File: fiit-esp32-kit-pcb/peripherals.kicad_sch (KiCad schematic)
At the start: 21 parts, among them Q2 SFH320, SW1 SPST NO, SW2 SPST NO, SW3 SPST NO, SW4 SPST NO, U4 AHT20

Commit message: footprints assignment
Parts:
- removed U4: AHT20, Findemm:AHT20, symbol Findemm:AHT20
- added U4: AHT20, FIIT_Kit:AHT20, symbol FIIT_Kit:AHT20
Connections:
- net +3.3V: now also U4.2 (VDD)
- net GND: now also U4.5 (GND)
- net SCL: now also U4.3 (SCL)
- net SDA: now also U4.4 (SDA)
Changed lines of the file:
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@@
+	)
+	(symbol
+		(lib_id "FIIT_Kit:AHT20")
+		(at 101.6 132.08 0)
+		(unit 1)
+		(exclude_from_sim no)
+		(in_bom yes)
+		(on_board yes)
+		(dnp no)
+		(property "Reference" "U4"
+			(at 93.726 121.412 0)
+			(effects
+				(font
+					(size 1.27 1.27)
+				)
+				(justify left)
+			)
+		)
+		(property "Value" "AHT20"
+			(at 93.726 123.444 0)
+			(effects
+				(font
+					(size 1.27 1.27)
+				)
+				(justify left)
+			)
+		)
+		(property "Footprint" "FIIT_Kit:AHT20"
+			(at 101.6 132.08 0)
+			(effects
+				(font
+					(size 1.27 1.27)
+				)
+				(justify bottom)
+				(hide yes)
+			)
+		)
+		(property "Datasheet" "https://files.seeedstudio.com/wiki/Grove-AHT20_I2C_Industrial_Grade_Temperature_and_Humidity_Sensor/AHT20-datasheet-2020-4-16.pdf"
+			(at 101.6 132.08 0)
+			(effects
+				(font
+					(size 1.27 1.27)
+				)
+				(hide yes)
+			)
+		)
+		(property "Description" ""
+			(at 101.6 132.08 0)
+			(effects
+				(font
+					(size 1.27 1.27)
+				)
+				(hide yes)
+			)
+		)
+		(property "LCSC" "C2757850"
+			(at 101.6 132.08 0)
+			(effects
+				(font
+					(size 1.27 1.27)
+				)
+				(hide yes)
+			)
+		)
+		(property "Manufacturer Part Number" "AHT20"
+			(at 101.6 132.08 0)
+			(effects
+				(font
+					(size 1.27 1.27)
+				)
+				(hide yes)
+			)
+		)
+		(pin "4"
+		)
+		(pin "3"
+		)
+		(pin "1"
+		)
+		(pin "2"
+		)
+		(pin "5"
+		)
+		(pin "6"
+		)
+		(instances
+			(project ""
+				(path "/d7013812-ce13-4db9-a6cc-42acdc5acaf9/fe4defb8-cb63-4770-8d91-1c7f8da70e07"
+					(reference "U4")
+					(unit 1)
+				)
+			)
+		)
 	)
 	(symbol
@@
 					(unit 1)
 				)
-			)
-		)
-	)
-	(symbol
-		(lib_id "Findemm:AHT20")
-		(at 101.6 132.08 0)
-		(unit 1)
-		(exclude_from_sim no)
-		(in_bom yes)
-		(on_board yes)
-		(dnp no)
-		(property "Reference" "U4"
-			(at 93.472 121.158 0)
-			(effects
-				(font
-					(size 1.27 1.27)
-				)
-				(justify left)
-			)
-		)
-		(property "Value" "AHT20"
-			(at 93.472 123.19 0)
-			(effects
-				(font
-					(size 1.27 1.27)
-				)
-				(justify left)
-			)
-		)
-		(property "Footprint" "Findemm:AHT20"
-			(at 101.6 132.08 0)
-			(effects
-				(font
-					(size 1.27 1.27)
-				)
-				(justify bottom)
-				(hide yes)
-			)
-		)
-		(property "Datasheet" "https://files.seeedstudio.com/wiki/Grove-AHT20_I2C_Industrial_Grade_Temperature_and_Humidity_Sensor/AHT20-datasheet-2020-4-16.pdf"
-			(at 101.6 132.08 0)
-			(effects
-				(font
-					(size 1.27 1.27)
-				)
-				(hide yes)
-			)
-		)
-		(property "Description" ""
-			(at 101.6 132.08 0)
-			(effects
-				(font
-					(size 1.27 1.27)
-				)
-				(hide yes)
-			)
-		)
-		(property "LCSC" "C2757850"
-			(at 101.6 132.08 0)
-			(effects
-				(font
-					(size 1.27 1.27)
-				)
-				(hide yes)
-			)
-		)
-		(property "Manufacturer Part Number" "AHT20"
-			(at 101.6 132.08 0)
-			(effects
-				(font
-					(size 1.27 1.27)
-				)
-				(hide yes)
-			)
-		)
-		(pin "2"
-		)
-		(pin "3"
-		)
-		(pin "4"
-		)
-		(pin "5"
-		)
-		(pin "1"
-		)
-		(pin "6"
-		)
-		(instances
-			(project "fiit-esp32-kit-pcb"
-				(path "/d7013812-ce13-4db9-a6cc-42acdc5acaf9/fe4defb8-cb63-4770-8d91-1c7f8da70e07"
-					(reference "U4")
-					(unit 1)
-				)

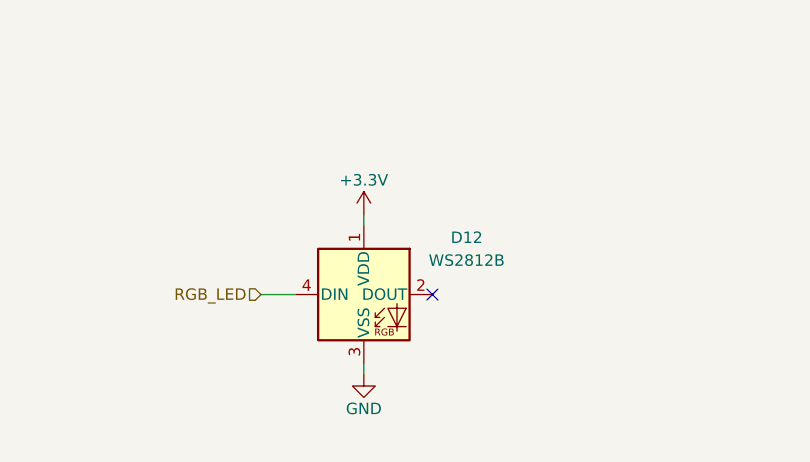
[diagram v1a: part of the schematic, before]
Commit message: updated manufacturer part numbers
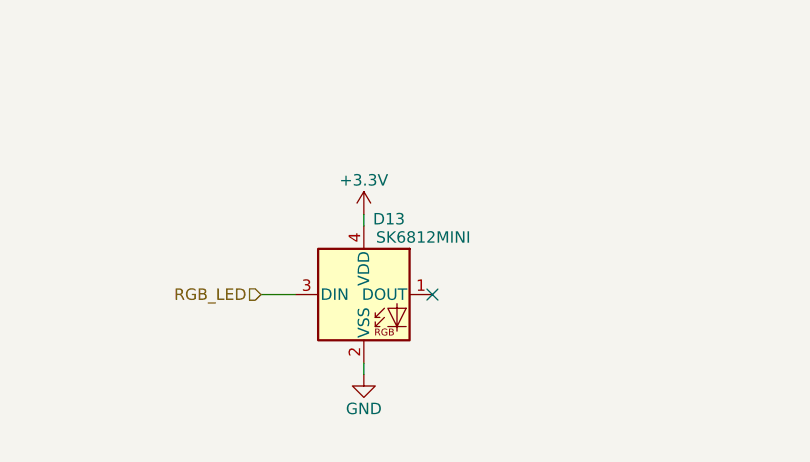
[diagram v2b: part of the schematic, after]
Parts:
- removed D12: WS2812B, LED_SMD:LED_WS2812B_PLCC4_5.0x5.0mm_P3.2mm, symbol LED:WS2812B
- added D13: SK6812MINI, LED_SMD:LED_SK6812MINI_PLCC4_3.5x3.5mm_P1.75mm, symbol LED:SK6812MINI
- Q2: footprint LED_SMD:LED_PLCC-2_3.4x3.0mm_KA -> FIIT_Kit:TEMT6000X01; LCSC (none) -> C94098; Manufacturer Part Number (none) -> TEMT6000X01
- R20, R21, R23, R26: LCSC (none) -> C22775; Manufacturer Part Number (none) -> 0603WAF1000T5E
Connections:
- net +3.3V: now also D13.4 (VDD)
- net GND: now also D13.2 (VSS)
- net RGB_LED: now also D13.3 (DIN)
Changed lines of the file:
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@@
 			)
 		)
-		(property "LCSC" ""
+		(property "LCSC" "C22775"
 			(at 152.4 60.96 0)
 			(effects
@@
 			)
 		)
-		(property "Manufacturer Part Number" ""
+		(property "Manufacturer Part Number" "0603WAF1000T5E"
 			(at 152.4 60.96 0)
 			(effects
@@
 			)
 		)
-		(property "LCSC" ""
+		(property "LCSC" "C22775"
 			(at 152.4 52.07 0)
 			(effects
@@
 			)
 		)
-		(property "Manufacturer Part Number" ""
+		(property "Manufacturer Part Number" "0603WAF1000T5E"
 			(at 152.4 52.07 0)
 			(effects
@@
 				(path "/d7013812-ce13-4db9-a6cc-42acdc5acaf9/fe4defb8-cb63-4770-8d91-1c7f8da70e07"
 					(reference "#PWR058")
-					(unit 1)
-				)
-			)
-		)
-	)
-	(symbol
-		(lib_id "LED:WS2812B")
-		(at 195.58 133.35 0)
-		(unit 1)
-		(exclude_from_sim no)
-		(in_bom yes)
-		(on_board yes)
-		(dnp no)
-		(fields_autoplaced yes)
-		(property "Reference" "D12"
-			(at 207.01 127.0314 0)
-			(effects
-				(font
-					(size 1.27 1.27)
-				)
-			)
-		)
-		(property "Value" "WS2812B"
-			(at 207.01 129.5714 0)
-			(effects
-				(font
-					(size 1.27 1.27)
-				)
-			)
-		)
-		(property "Footprint" "LED_SMD:LED_WS2812B_PLCC4_5.0x5.0mm_P3.2mm"
-			(at 196.85 140.97 0)
-			(effects
-				(font
-					(size 1.27 1.27)
-				)
-				(justify left top)
-				(hide yes)
-			)
-		)
-		(property "Datasheet" "https://cdn-shop.adafruit.com/datasheets/WS2812B.pdf"
-			(at 198.12 142.875 0)
-			(effects
-				(font
-					(size 1.27 1.27)
-				)
-				(justify left top)
-				(hide yes)
-			)
-		)
-		(property "Description" "RGB LED with integrated controller"
-			(at 195.58 133.35 0)
-			(effects
-				(font
-					(size 1.27 1.27)
-				)
-				(hide yes)
-			)
-		)
-		(pin "3"
-		)
-		(pin "1"
-		)
-		(pin "2"
-		)
-		(pin "4"
-		)
-		(instances
-			(project "fiit-esp32-kit-pcb"
-				(path "/d7013812-ce13-4db9-a6cc-42acdc5acaf9/fe4defb8-cb63-4770-8d91-1c7f8da70e07"
-					(reference "D12")
 					(unit 1)
 				)
@@
 			)
 		)
-		(property "LCSC" ""
+		(property "LCSC" "C22775"
 			(at 152.4 69.85 0)
 			(effects
@@
 			)
 		)
-		(property "Manufacturer Part Number" ""
+		(property "Manufacturer Part Number" "0603WAF1000T5E"
 			(at 152.4 69.85 0)
 			(effects
@@
 			)
 		)
-		(property "LCSC" ""
+		(property "LCSC" "C22775"
 			(at 152.4 78.74 0)
 			(effects
@@
 			)
 		)
-		(property "Manufacturer Part Number" ""
+		(property "Manufacturer Part Number" "0603WAF1000T5E"
 			(at 152.4 78.74 0)
 			(effects
@@
 				(path "/d7013812-ce13-4db9-a6cc-42acdc5acaf9/fe4defb8-cb63-4770-8d91-1c7f8da70e07"
 					(reference "R22")
+					(unit 1)
+				)
+			)
+		)
+	)
+	(symbol
+		(lib_id "LED:SK6812MINI")
+		(at 195.58 133.35 0)
+		(unit 1)
+		(exclude_from_sim no)
+		(in_bom yes)
+		(on_board yes)
+		(dnp no)
+		(property "Reference" "D13"
+			(at 198.374 124.968 0)
+			(effects
+				(font
+					(size 1.27 1.27)
+				)
+			)
+		)
+		(property "Value" "SK6812MINI"
+			(at 202.184 127 0)
+			(effects
+				(font
+					(size 1.27 1.27)
+				)
+			)
+		)
+		(property "Footprint" "LED_SMD:LED_SK6812MINI_PLCC4_3.5x3.5mm_P1.75mm"
+			(at 196.85 140.97 0)
+			(effects
+				(font
+					(size 1.27 1.27)
+				)
+				(justify left top)
+				(hide yes)
+			)
+		)
+		(property "Datasheet" "https://cdn-shop.adafruit.com/product-files/2686/SK6812MINI_REV.01-1-2.pdf"
+			(at 198.12 142.875 0)
+			(effects
+				(font
+					(size 1.27 1.27)
+				)
+				(justify left top)
+				(hide yes)
+			)
+		)
+		(property "Description" "RGB LED with integrated controller"
+			(at 195.58 133.35 0)
+			(effects
+				(font
+					(size 1.27 1.27)
+				)
+				(hide yes)
+			)
+		)
+		(property "LCSC" "C2886570"
+			(at 195.58 133.35 0)
+			(effects
+				(font
+					(size 1.27 1.27)
+				)
+				(hide yes)
+			)
+		)
+		(property "Manufacturer Part Number" "SK6812mini"
+			(at 195.58 133.35 0)
+			(effects
+				(font
+					(size 1.27 1.27)
+				)
+				(hide yes)
+			)
+		)
+		(pin "3"
+		)
+		(pin "2"
+		)
+		(pin "1"
+		)
+		(pin "4"
+		)
+		(instances
+			(project ""
+				(path "/d7013812-ce13-4db9-a6cc-42acdc5acaf9/fe4defb8-cb63-4770-8d91-1c7f8da70e07"
+					(reference "D13")
 					(unit 1)
 				)
@@
 			)
 		)
-		(property "Footprint" "LED_SMD:LED_PLCC-2_3.4x3.0mm_KA"
+		(property "Footprint" "FIIT_Kit:TEMT6000X01"
 			(at 238.252 64.516 0)
 			(effects
@@
 			(at 226.06 60.96 0)
 			(effects
+				(font
+					(size 1.27 1.27)
+				)
+				(hide yes)
+			)
+		)
+		(property "LCSC" "C94098"
+			(at 226.06 60.96 0)
+			(effects
+				(font
+					(size 1.27 1.27)
+				)
+				(hide yes)
+			)
+		)
+		(property "Manufacturer Part Number" "TEMT6000X01"
+			(at 226.06 60.96 0)
+			(effects

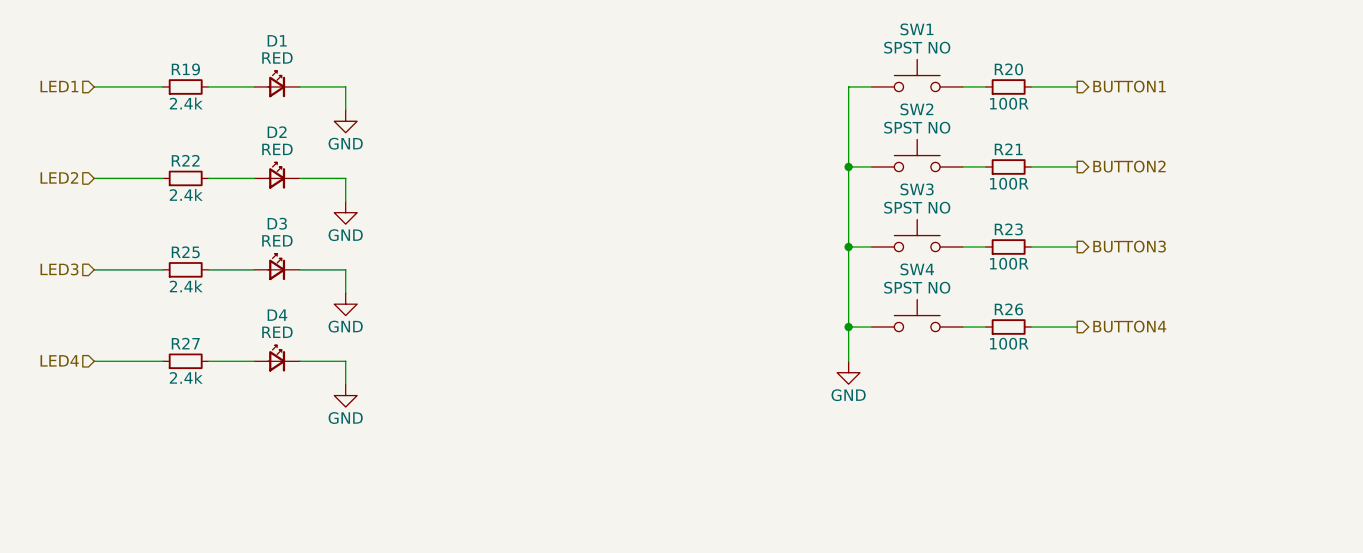
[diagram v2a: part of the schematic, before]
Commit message: component placement
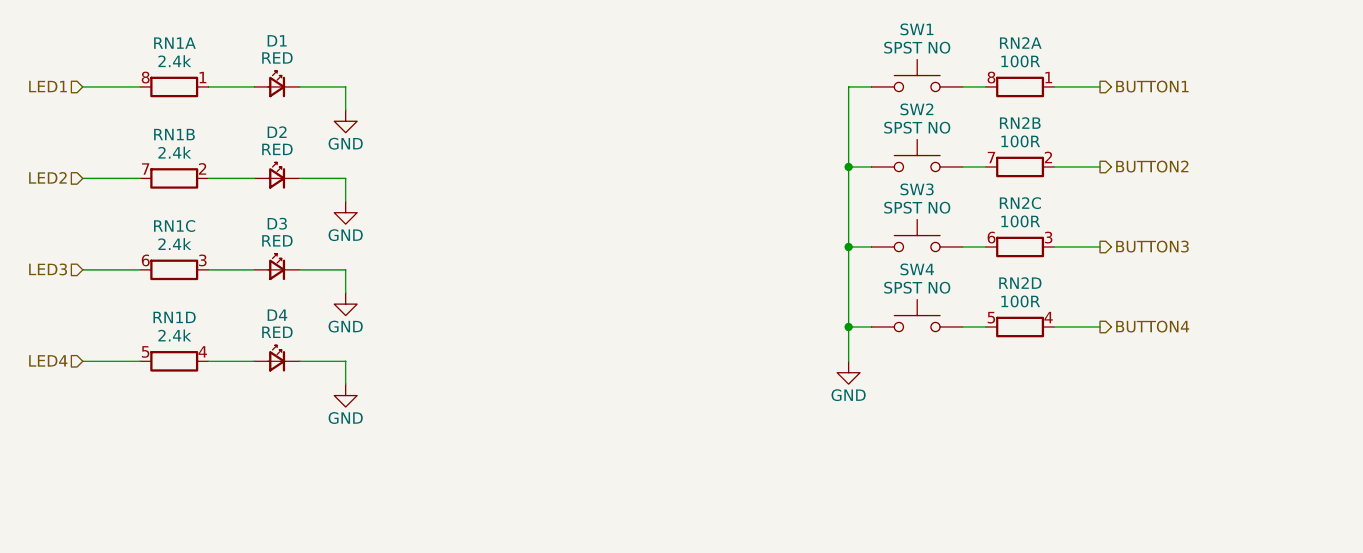
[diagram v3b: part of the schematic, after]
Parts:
- removed R19, R22, R25, R27: 2.4k, Resistor_SMD:R_0603_1608Metric, symbol Device:R_Small
- removed R20, R21, R23, R26: 100R, Resistor_SMD:R_0603_1608Metric, symbol Device:R_Small
- added RN1: 2.4k, Resistor_SMD:R_Array_Convex_4x0603, symbol Device:R_Pack04_Split
- added RN2: 100R, Resistor_SMD:R_Array_Convex_4x0603, symbol Device:R_Pack04_Split
- SW1, SW2, SW3, SW4: footprint Button_Switch_SMD:SW_SPST_TL3342 -> Button_Switch_SMD:SW_SPST_PTS647_Sx38
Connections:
- net BUTTON1: now also RN2.1 (R1.1)
- net BUTTON2: now also RN2.2 (R2.1)
- net BUTTON3: now also RN2.3 (R3.1)
- net BUTTON4: now also RN2.4 (R4.1)
- net LED1: now also RN1.8 (R1.2)
- net LED2: now also RN1.7 (R2.2)
- net LED3: now also RN1.6 (R3.2)
- net LED4: now also RN1.5 (R4.2)
- net at D4.2 (A): now also RN1.4 (R4.1)
- net at D3.2 (A): now also RN1.3 (R3.1)
- net at SW3.2: now also RN2.6 (R3.2)
- net at D1.2 (A): now also RN1.1 (R1.1)
- net at SW2.2: now also RN2.7 (R2.2)
- net at SW1.2: now also RN2.8 (R1.2)
- net at D2.2 (A): now also RN1.2 (R2.1)
- net at SW4.2: now also RN2.5 (R4.2)
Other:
- company: STU FIIT -> FIIT STU

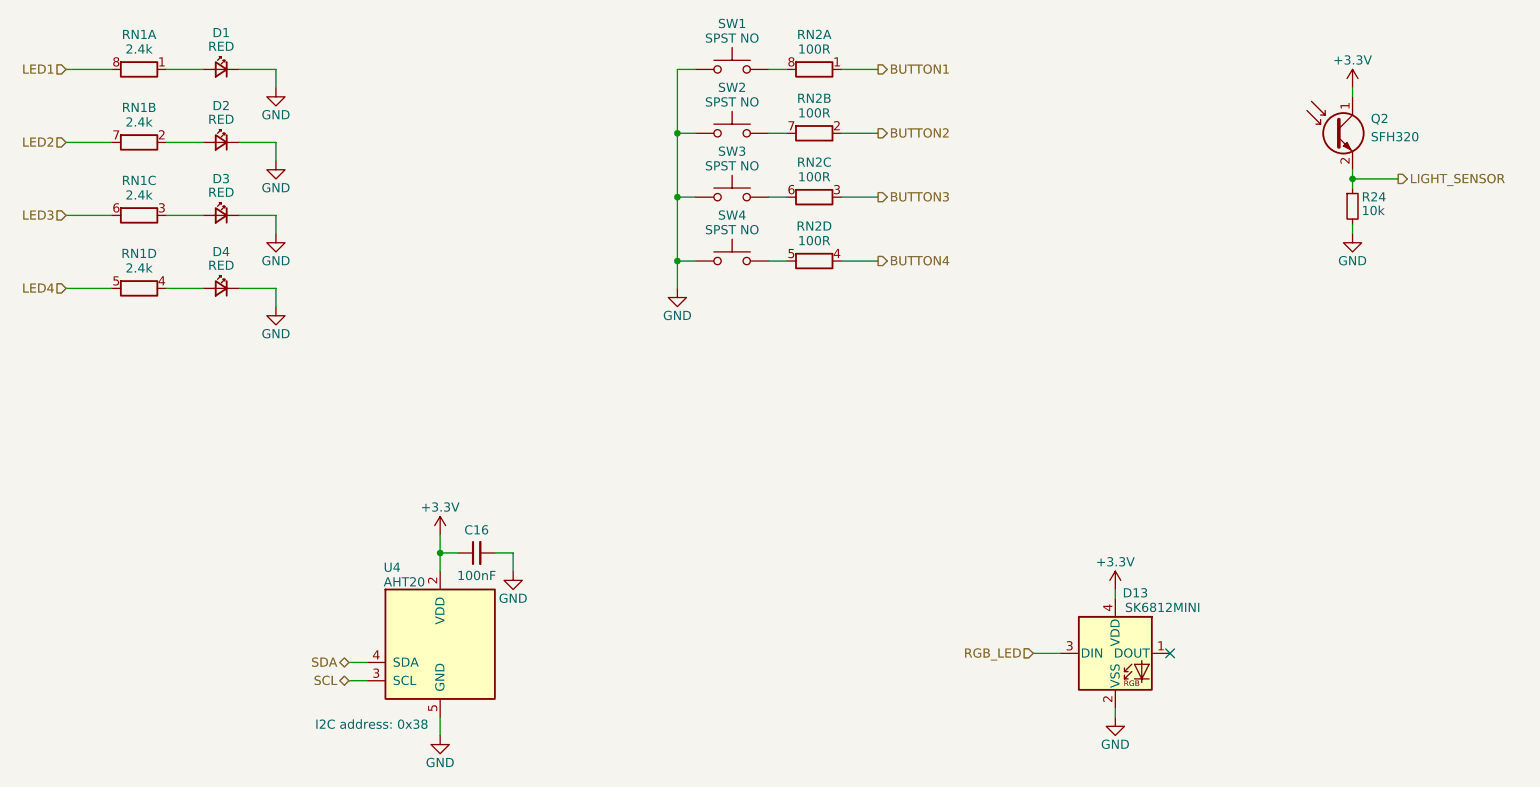
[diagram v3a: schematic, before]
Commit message: updated components placement (unrouted 237)
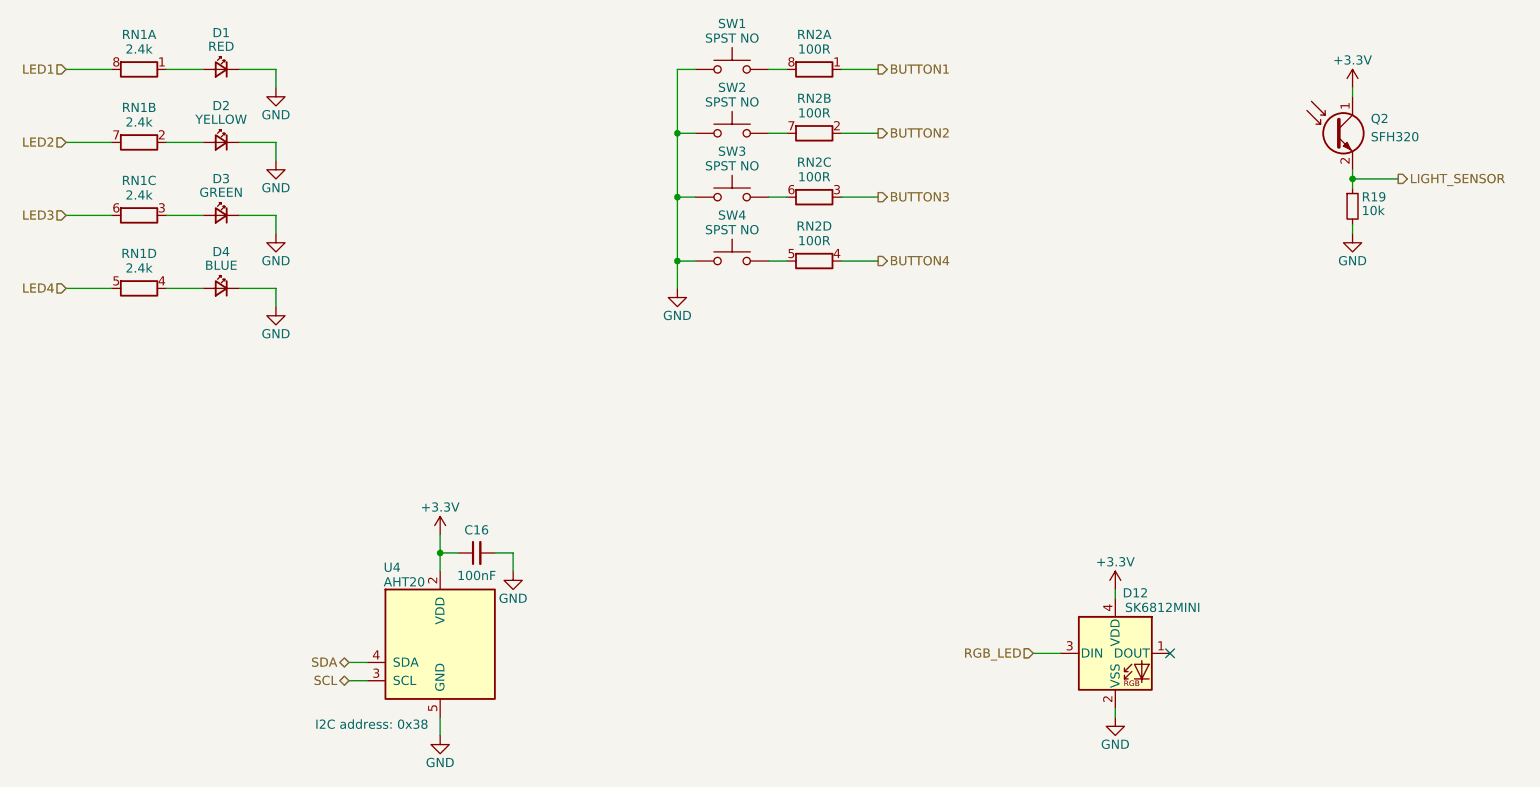
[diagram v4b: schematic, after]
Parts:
- D1: LCSC C434431 -> C2295; Manufacturer Part Number SZYY0805R -> KT-0805R
- D2: value RED -> YELLOW; LCSC C434431 -> C2296; Manufacturer Part Number SZYY0805R -> KT-0805Y
- D3: value RED -> GREEN; LCSC C434431 -> C2297; Manufacturer Part Number SZYY0805R -> KT-0805G
- D4: value RED -> BLUE; LCSC C434431 -> C2293; Manufacturer Part Number SZYY0805R -> KT-0805B
- renumbered D13 to D12, R24 to R19
